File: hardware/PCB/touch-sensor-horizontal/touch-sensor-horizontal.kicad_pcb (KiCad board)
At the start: 2 copper layers, 302.2 x 54.4 mm, 1 part

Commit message: removed dropped ideas, re organised datasheets, created project for integrated touch sensor
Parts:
- added J1: Conn_01x30, touch-sensors:tstick-buttons, F.Cu at (56.9, 154.4)
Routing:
- net /TOUCH2: track 136.7 -> 149.8 mm
- net /TOUCH8: track 81.2 -> 94.2 mm
- net /TOUCH27: track 142.4 -> 131.6 mm
- net /TOUCH28: track 151.8 -> 141.1 mm
- net /TOUCH26: track 133.0 -> 123.1 mm
- net /TOUCH25: track 123.9 -> 114.5 mm
- net /TOUCH29: track 160.7 -> 169.8 mm
- net /TOUCH24: track 114.4 -> 105.7 mm
- net /TOUCH23: track 105.7 -> 97.0 mm
- net /TOUCH22: track 96.8 -> 88.5 mm
- net /TOUCH21: track 86.9 -> 79.8 mm
- net /TOUCH20: track 77.7 -> 71.2 mm
- net /TOUCH19: track 68.3 -> 62.5 mm
- net /TOUCH1: track 146.4 -> 140.8 mm
- net /TOUCH18: track 59.0 -> 53.9 mm
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- added copper zone on F.Cu, net GND
- removed copper zone on B.Cu, net /TOUCH0
- removed copper zone on B.Cu, net /TOUCH1
- removed copper zone on B.Cu, net /TOUCH10
- removed copper zone on B.Cu, net /TOUCH11
- removed copper zone on B.Cu, net /TOUCH12
- removed copper zone on B.Cu, net /TOUCH13
- removed copper zone on B.Cu, net /TOUCH14
- removed copper zone on B.Cu, net /TOUCH15
- removed copper zone on B.Cu, net /TOUCH16
- removed copper zone on B.Cu, net /TOUCH17
- removed copper zone on B.Cu, net /TOUCH18
- removed copper zone on B.Cu, net /TOUCH19
- removed copper zone on B.Cu, net /TOUCH2
- removed copper zone on B.Cu, net /TOUCH20
- removed copper zone on B.Cu, net /TOUCH21
- removed copper zone on B.Cu, net /TOUCH22
- removed copper zone on B.Cu, net /TOUCH23
- removed copper zone on B.Cu, net /TOUCH24
- removed copper zone on B.Cu, net /TOUCH25
- removed copper zone on B.Cu, net /TOUCH26
- removed copper zone on B.Cu, net /TOUCH27
- removed copper zone on B.Cu, net /TOUCH28
- removed copper zone on B.Cu, net /TOUCH29
- removed copper zone on B.Cu, net /TOUCH3
- removed copper zone on B.Cu, net /TOUCH4
- removed copper zone on B.Cu, net /TOUCH5
- removed copper zone on B.Cu, net /TOUCH6
- removed copper zone on B.Cu, net /TOUCH7
- removed copper zone on B.Cu, net /TOUCH8
- removed copper zone on B.Cu, net /TOUCH9
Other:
- board size 302.2 x 54.4 mm -> 302 x 56.5 mm

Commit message: rerouted touch sensor so that traces don't run under sensor pad, removed rigid flex pcb design as it will be more hassle than it is worths
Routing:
- net /TOUCH8: track 94.2 -> 73.2 mm
- net /TOUCH29: track 169.8 -> 149.0 mm
- net /TOUCH2: track 149.8 -> 129.7 mm
- net /TOUCH13: track 36.6 -> 26.2 mm
- net /TOUCH16: track 36.4 -> 26.4 mm
- net /TOUCH12: track 45.4 -> 35.5 mm
- net /TOUCH17: track 45.3 -> 35.8 mm
- net /TOUCH14: track 27.9 -> 18.7 mm
- net /TOUCH11: track 54.1 -> 44.9 mm
- net /TOUCH15: track 27.7 -> 18.5 mm
- net /TOUCH18: track 53.9 -> 45.2 mm
- net /TOUCH10: track 62.7 -> 54.3 mm
- net /TOUCH19: track 62.5 -> 54.7 mm
- net /TOUCH9: track 70.9 -> 63.7 mm
- net /TOUCH20: track 71.2 -> 64.0 mm
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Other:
- outline, holes or cut-outs redrawn

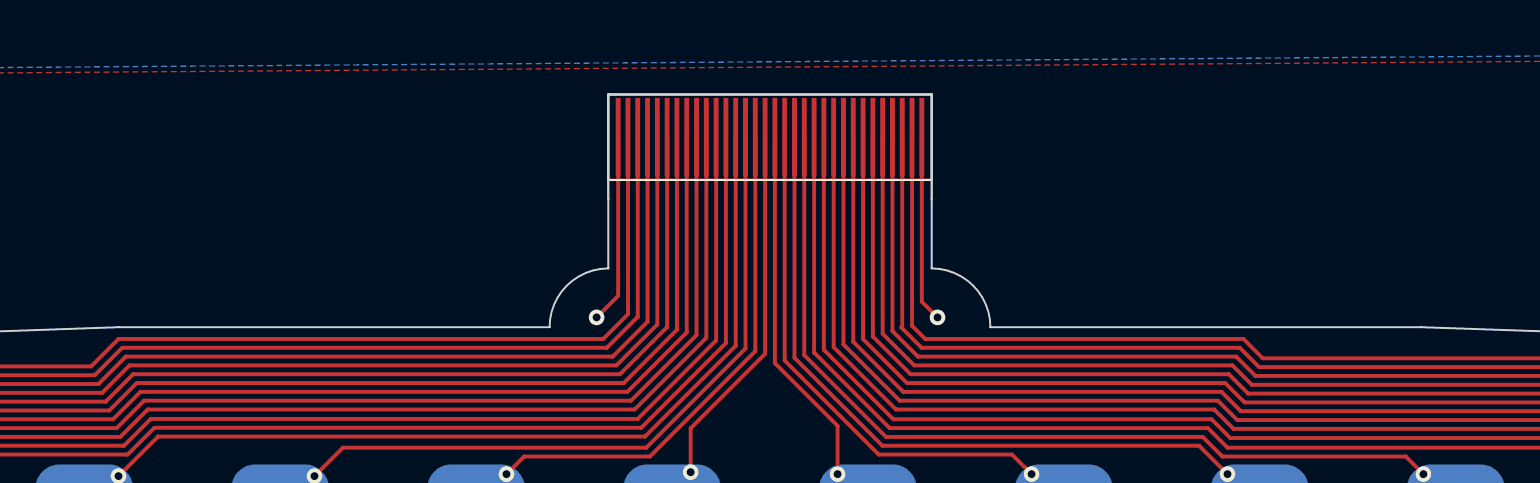
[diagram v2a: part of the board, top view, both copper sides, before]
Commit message: added up to date gerber files, switched ground plane to hatched plane for reduced parasitic capacitance in touch board
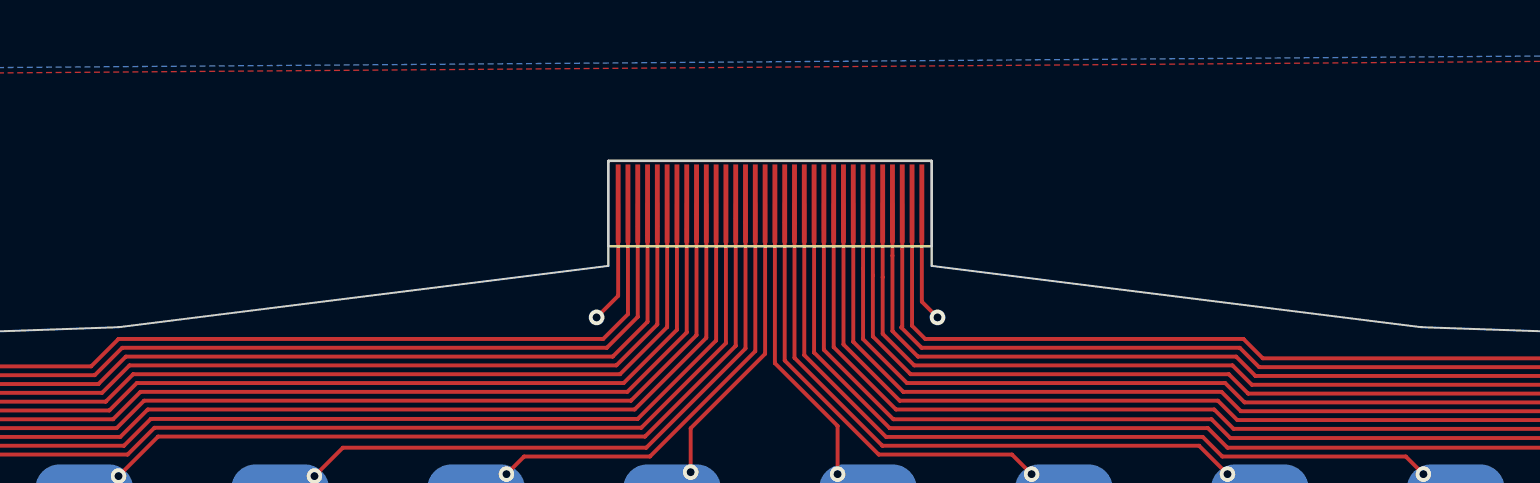
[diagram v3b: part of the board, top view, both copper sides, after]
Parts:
- moved C1 3.39 mm to (201.8, 121.1)
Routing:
- net GND: track 19.2 -> 12.4 mm
- net /TOUCH1: track 139.0 -> 135.7 mm
- net /TOUCH3: track 120.3 -> 117.0 mm
- net /TOUCH26: track 120.6 -> 117.2 mm
- net /TOUCH2: track 129.7 -> 126.3 mm
- net /TOUCH16: track 26.4 -> 23.0 mm
- net /TOUCH15: track 18.5 -> 15.1 mm
- net /TOUCH9: track 63.7 -> 60.3 mm
- net /TOUCH8: track 73.2 -> 69.8 mm
- net /TOUCH5: track 101.3 -> 97.9 mm
- net /TOUCH4: track 110.8 -> 107.5 mm
- net /TOUCH29: track 149.0 -> 145.6 mm
- net /TOUCH28: track 139.4 -> 136.0 mm
- net /TOUCH25: track 111.1 -> 107.7 mm
- net /TOUCH24: track 101.7 -> 98.3 mm
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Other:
- board size 302 x 56.5 mm -> 302 x 53.1 mm
